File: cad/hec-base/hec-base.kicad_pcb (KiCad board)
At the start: 4 copper layers, 47.8 x 47.8 mm, 140 parts, among them IC201 LMR14206, IC202 LTC3406ES5, IC203 74LVC1G57, IC204 TPS3307-33, IC205 STM32F103C8Tx, IC301 MAX485E, IC302 74LVC1G57, IC501 DS2482S-100, IC502 DS18B20, IC503 DS28E25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

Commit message: MT-Marienkaefer: Schaltregler von Platinenkante verschoben.
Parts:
- moved C205 1.85 mm to (123.9, 111.3)
- moved C208 1.85 mm to (117.4, 110.5)
- moved C209 1.85 mm to (115.6, 110.7)
- moved C210 1.85 mm to (113.5, 110.7)
- moved IC202 1.85 mm to (121.1, 111.1)
- moved L202 1.85 mm to (120.7, 111.2)
- moved R205 1.85 mm to (120.6, 107.8)
- moved R207 1.85 mm to (118.1, 108.6)
- moved FID106 1.12 mm to (115.7, 113.7)
- moved C211 1.02 mm to (121.6, 108.0)
- moved C215 0.80 mm to (117.5, 105.8), turned to 0 degrees
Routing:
- net GNDD: track 212.6 -> 196.7 mm, vias 73 -> 75
- net Net-(C208-Pad2): track 18.6 -> 14.3 mm, vias 1 -> 2
- net +5V: track 90.8 -> 94.6 mm
- net Net-(C211-Pad1): track 7.53 -> 9.54 mm
- net Net-(C215-Pad2): track 6.78 -> 8.36 mm

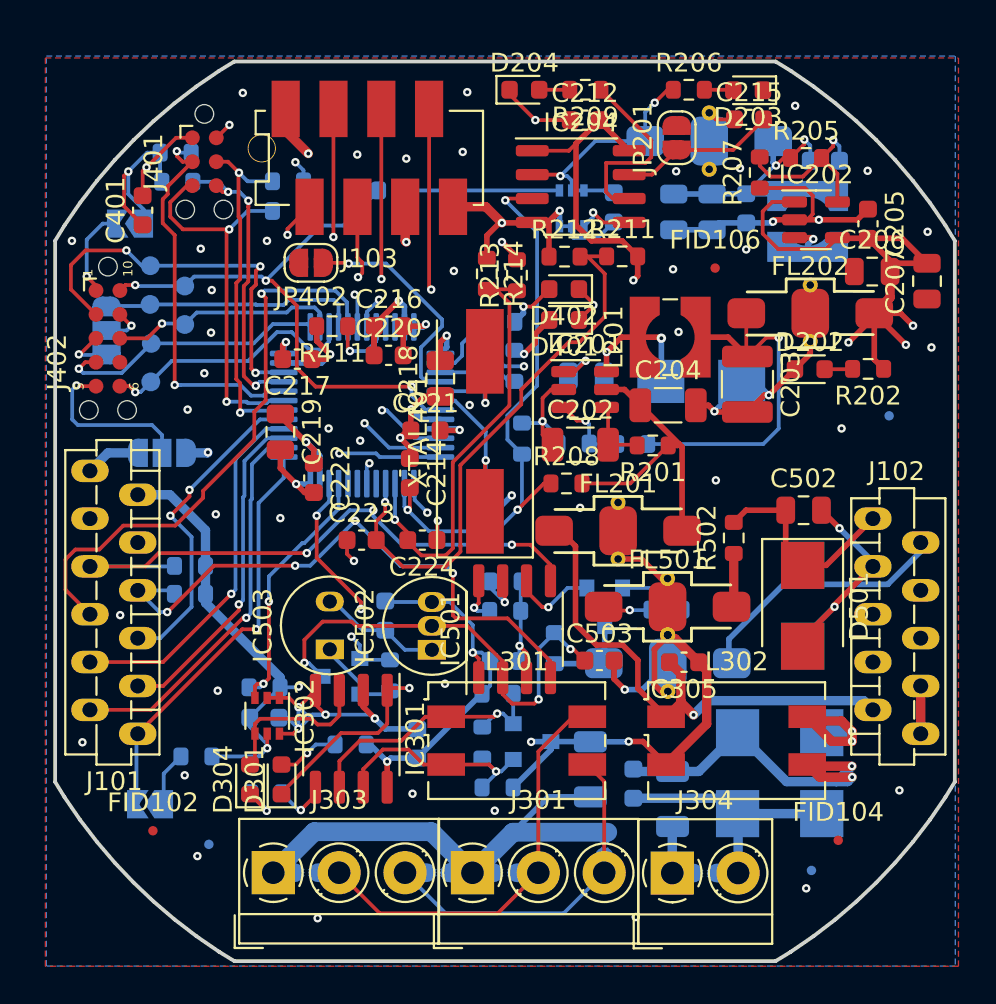
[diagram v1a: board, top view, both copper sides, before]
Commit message: Alle in-akzeptablen DRC-Fehler im Layout behoben.
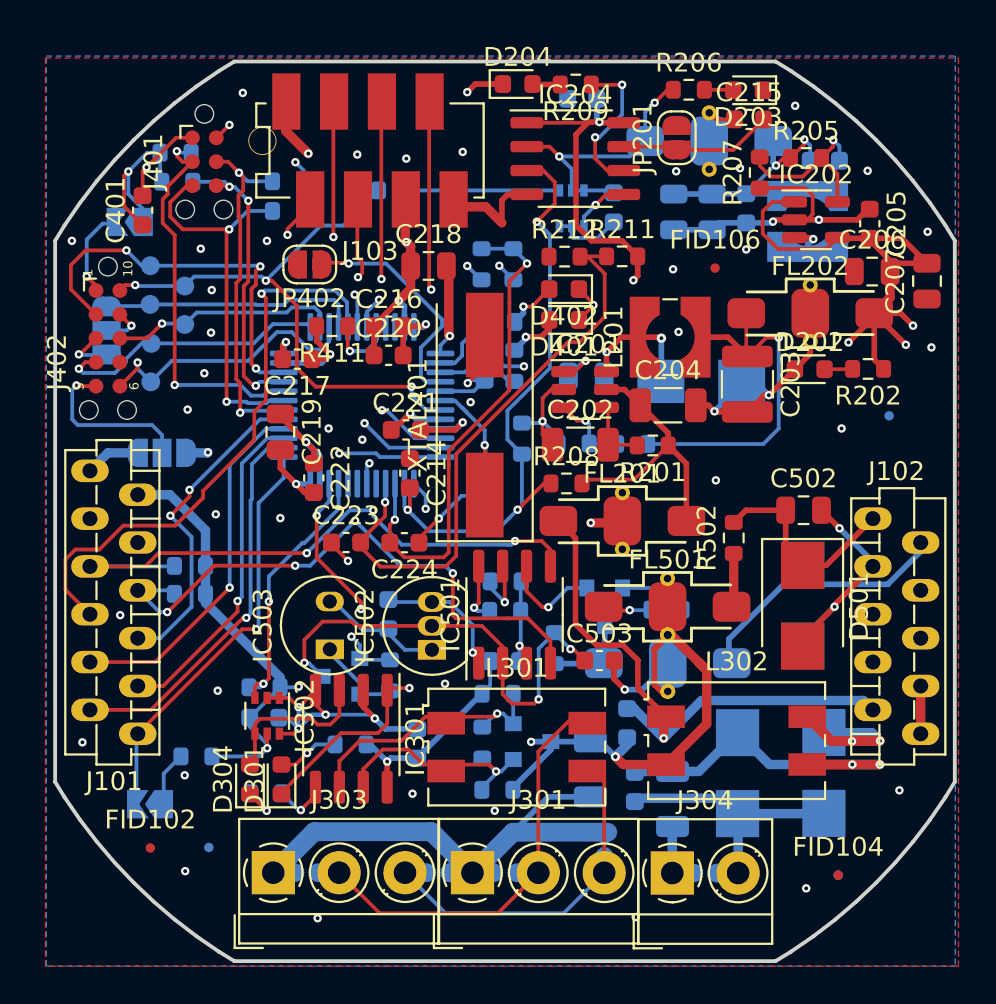
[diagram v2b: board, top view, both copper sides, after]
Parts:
- C212, C305, R213, R214: moved to B.Cu
- moved C218 6.01 mm to (100.5, 113.6), turned to 0 degrees
- moved C305 4.43 mm to (111.1, 137.9), turned to 90 degrees
- moved FID104 1.85 mm to (122.3, 145.9)
- moved IC204 1.51 mm to (108.3, 107.9)
- moved FID103 1.44 mm to (122.3, 145.9)
- moved C212 1.14 mm to (108.7, 104.7)
- moved C221 1.04 mm to (99.3, 122.3)
- moved C224 0.96 mm to (99.2, 128.3)
- moved FID102 0.93 mm to (85.7, 144.5)
- moved XTAL401 0.86 mm to (103.5, 121.5)
- moved C402 0.84 mm to (103.5, 125.0)
- moved C223 0.84 mm to (96.1, 128.3)
- moved IC501 0.77 mm to (105.1, 132.1)
- moved R213 0.61 mm to (105.0, 113.5), turned to 270 degrees
- moved R214 0.58 mm to (103.3, 113.5), turned to 90 degrees
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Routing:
- net +3V3: track 47.1 -> 51.8 mm
- net Net-(D303-Pad1): track 9.59 -> 13.9 mm
- net GNDD: track 196.7 -> 192.8 mm, vias 75 -> 71
- net /Stromversorgung/Vcc3V3SNS_1.20Vref: track 23.7 -> 26.7 mm, vias 1 -> 2
- net Net-(IC204-Pad6): track 10.1 -> 8.07 mm, vias 0 -> 2
- net /Stromversorgung/Vcc5VSNS_1.20Vref: track 30.0 -> 31.9 mm
- net +24V: track 27.9 -> 29.5 mm
- net /Stromversorgung/Vcc24VSNS_1.25Vref: track 31.5 -> 33.0 mm
- net /Microcontroller/PA3_GPIO_U2RX_AIN3: track 27.6 -> 26.3 mm
- net /Stromversorgung/Vcc24V: track 15.8 -> 14.7 mm
- net Net-(C302-Pad2): track 19.9 -> 21.0 mm
- net /Microcontroller/TDO: track 13.9 -> 14.9 mm
- net Net-(IC501-Pad8): track 2.43 -> 3.20 mm
- net Net-(IC501-Pad7): track 2.61 -> 3.39 mm
- net Net-(IC501-Pad6): track 4.53 -> 5.31 mm
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
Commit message: Texte für Silkscreen und Bestückungsplan platziert.
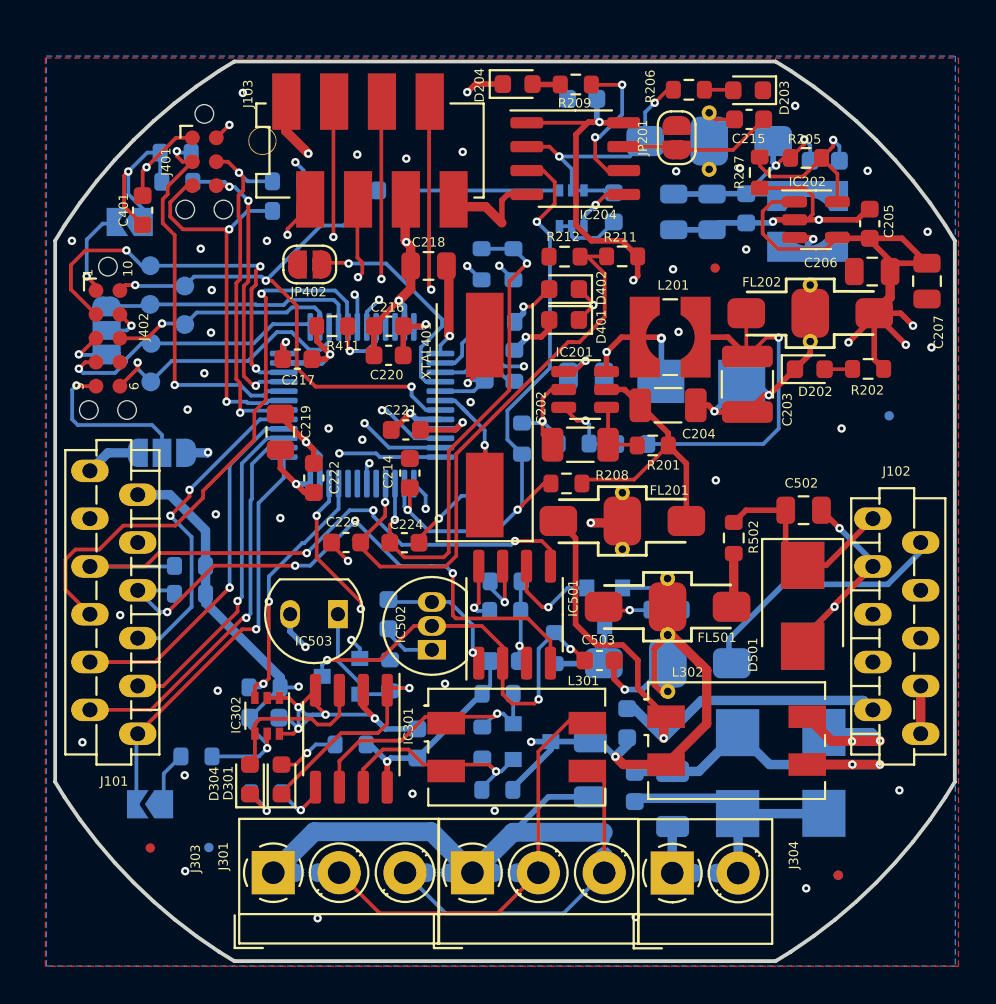
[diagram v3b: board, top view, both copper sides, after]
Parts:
- C201: value 1uF 50V X5R X7R -> 1uF 50V
- C202, C204: value 10uF 50V X5R X7R -> 10uF 50V
- C203: value 47uF 10V X5R X7R -> 47uF 10V
- C206, C207, C209, C210, C218, C219: value 4.7uF 10V X5R X7R -> 4.7uF 10V
- D401: value LED rot -> LED
- D402: value LED gruen -> LED
- L201: value 15uH, 1A WE 744053150 -> 15uH, 1A
- L202: value 2,5uH, 1,25A, 0R05 WE 744031002 -> 2,5uH, 1,25A
- moved IC503 1.92 mm to (95.7, 132.1), turned to 180 degrees
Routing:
- net /One-Wire-Devices/1Wire_5V: track 24.9 -> 22.5 mm
- net /One-Wire-Devices/1Wire_3V3: track 4.72 -> 6.41 mm
- net GNDD: track 192.8 -> 191.2 mm
- net Net-(E301-Pad2): track 33.3 -> 31.9 mm
